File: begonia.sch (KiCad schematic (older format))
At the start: 13 parts, among them J1 NEIGHBOR1, J2 NEIGHBOR2, J7 BONUS_ROW, P1 POGOPINS, SW1 SPST

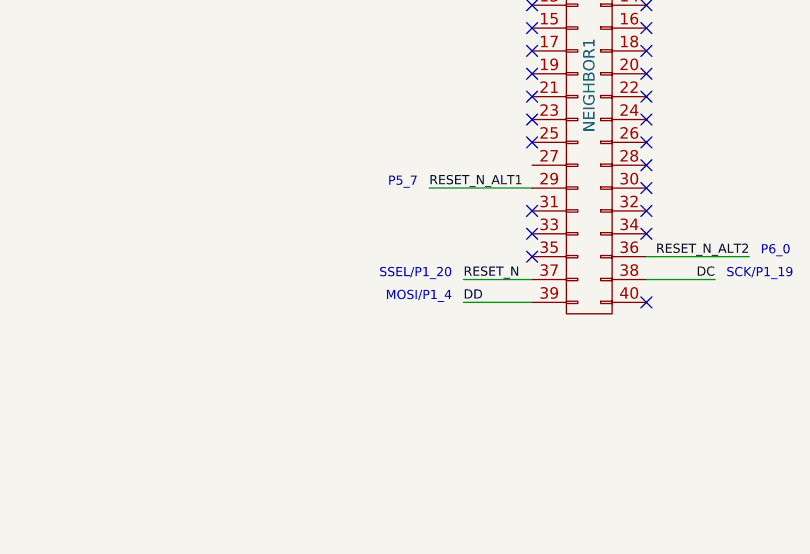
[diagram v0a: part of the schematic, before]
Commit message: adopt OSHWA convention for SPI signal names https://www.oshwa.org/a-resolution-to-redefine-spi-signal-names
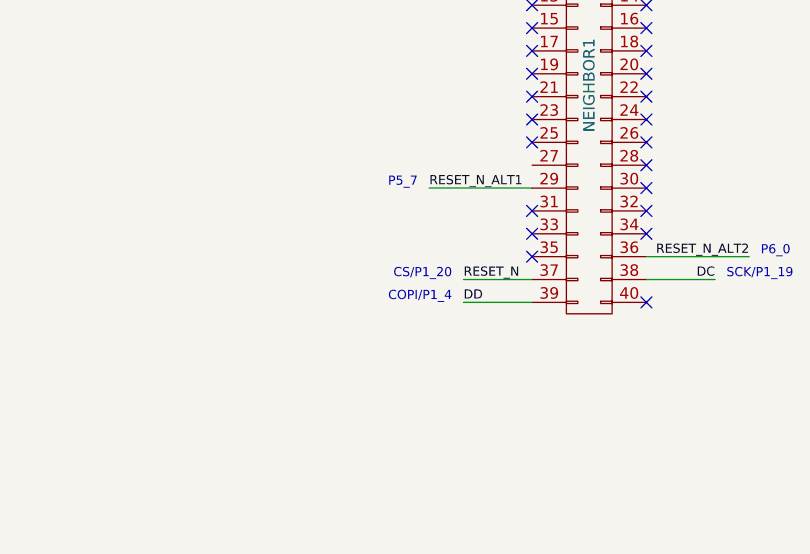
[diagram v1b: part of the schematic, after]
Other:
- note added: "COPI/P1_4"
- note added: "CS/P1_20"
- note removed: "MOSI/P1_4"
- note removed: "SSEL/P1_20"
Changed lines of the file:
@@
 RESET_N
 Text Notes 8550 6200 2    40   ~ 0
-MOSI/P1_4
+COPI/P1_4
 Text Notes 9750 6100 0    40   ~ 0
 SCK/P1_19
 Text Notes 8550 6100 2    40   ~ 0
-SSEL/P1_20
+CS/P1_20
 Wire Wire Line
 	8700 4300 8900 4300
